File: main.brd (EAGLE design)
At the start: 50.8 x 50.8 mm, 84 parts, among them Q1 5.8A/30V/35mΩ, Q2 5.8A/30V/35mΩ, Q3 2.5A/30V/105mΩ, U2 SN65HVD32_D_8

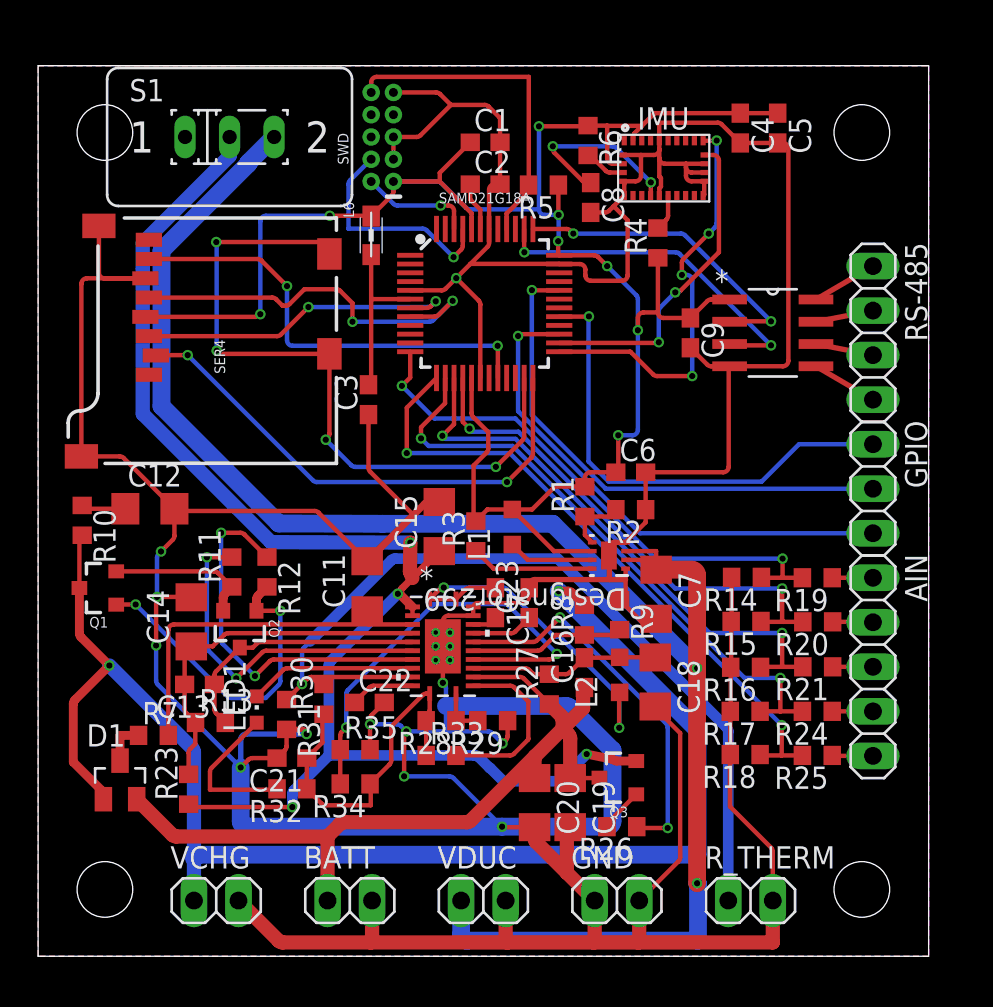
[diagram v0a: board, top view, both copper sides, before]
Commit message: Reworked Layout, added thermocouple ics
Second attempt at a board layout, more balanced spacing.
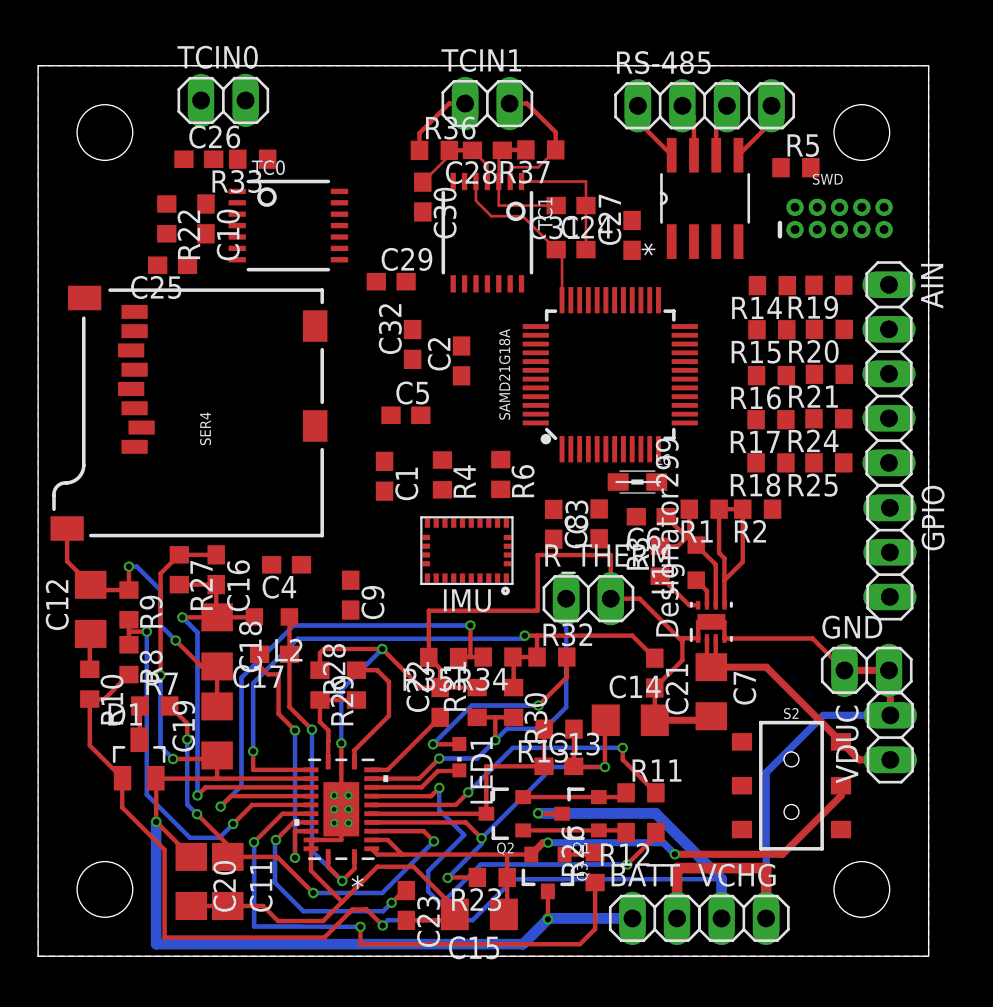
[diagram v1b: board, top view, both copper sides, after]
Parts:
- removed S1: (no value), switch:M251
- added C10, C24, C27, C28, C29, C32: 100nF, resistor:C0603
- added C25, C26, C30, C31: 10nF, resistor:C0603
- added R22, R36, R37: 100, resistor:R0603
- added S2: (no value), SparkFun-Switches:SWITCH_DPDT_SMD_AYZ0202
- added TC0, TC1: MAX31856, microbuilder:TSSOP14
- added TCIN0, TCIN1: (no value), pinhead:1X02
- R33: value 0 -> 100
- moved C4 35.9 mm to (14.2, 22.3), turned to 180 degrees
- moved R33 35.7 mm to (12.2, 45.5), turned to 180 degrees
- moved Q1 30.4 mm to (31.0, 8.13)
- moved VCHG 30.1 mm to (40.3, 2.16)
- moved R9 28.0 mm to (5.18, 20.0)
- moved C5 26.8 mm to (21.0, 30.9), turned to 0 degrees
- moved R11 26.5 mm to (34.4, 9.32), turned to 0 degrees
- moved SWD 26.5 mm to (45.7, 42.1), turned to 0 degrees
- moved R8 26.1 mm to (5.18, 16.9), turned to 270 degrees
- moved R12 26.0 mm to (34.4, 7.06), turned to 180 degrees
- moved C14 25.7 mm to (33.8, 13.5), turned to 0 degrees
- moved C18 25.1 mm to (10.2, 17.9)
- moved VDUC 25.0 mm to (48.6, 12.5), turned to 90 degrees
- moved IMU 24.5 mm to (24.5, 23.1), turned to 180 degrees
- moved C9 24.5 mm to (17.8, 20.6)
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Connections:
- removed net PC_CELL: POWER_CONTROLLER.14, R33.2
- new net N$21: C10.1, C26.2, R33.2, TC0.3
- new net N$22: C10.2, C25.1, R22.2, TC0.4
- new net N$23: R33.1, TC0.2, TCIN0.2
- new net N$24: R22.1, TCIN0.1
- new net N$25: C28.1, C31.2, R37.2, TC1.3
- new net N$26: C28.2, C30.1, R36.2, TC1.4
- new net N$27: R37.1, TC1.2, TCIN1.2
- new net N$28: R36.1, TCIN1.1
- new net TC0_CS: TC0.9
- new net TC0_DRDY: TC0.7
- new net TC0_FAULT: TC0.13
- new net TC1_CS: TC1.9
- new net TC1_DRDY: TC1.7
- new net TC1_FAULT: TC1.13
- net 3.3V: now also C24.1, C27.1, C29.1, C32.1, TC0.5, TC0.8, TC1.5, TC1.8
- net AIN0: no longer SAMD21G18A.12
- net AIN1: no longer SAMD21G18A.16
- net AIN2: no longer SAMD21G18A.15
- net AIN3: no longer SAMD21G18A.14
- net AIN4: no longer SAMD21G18A.13
- net GND: now also C24.2, C25.2, C26.1, C27.2, C29.2, C30.2, C31.1, C32.2, TC0.1, TC0.14, TC1.1, TC1.14
- net GPIO1: no longer SAMD21G18A.29
- net GPIO2: no longer SAMD21G18A.32
- net GPIO3: no longer SAMD21G18A.27
- net PB08D_SER4_P0: now also TC0.12, TC1.12
- net PB09D_SER4_P1: now also TC0.10, TC1.10
- net PB11D_SER4_P3: now also TC0.11, TC1.11
- net PC_PVCC: now also S2.2; no longer S1.2
- net PC_VREF: now also POWER_CONTROLLER.14; no longer R33.1
- net VSYS: now also S2.1; no longer S1.3
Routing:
- net GND: track 359.1 -> 154.6 mm, vias 12 -> 4
- net 3.3V: track 116.9 -> 19.6 mm, vias 8 -> 0
- net VSYS: track 98.2 -> 15.9 mm, vias 2 -> 0
- net PC_PVCC: track 82.6 -> 35.0 mm, vias 4 -> 2
- net PA14_PORT: track 40.7 -> 0.00 mm, vias 4 -> 0
- net AIN4: track 37.0 -> 0.00 mm, vias 2 -> 0
- net AIN3: track 34.5 -> 0.00 mm, vias 2 -> 0
- net AIN2: track 32.0 -> 0.00 mm, vias 2 -> 0
- net AIN0: track 31.4 -> 0.00 mm, vias 2 -> 0
- net GPIO2: track 29.9 -> 0.00 mm, vias 1 -> 0
- net GPIO3: track 29.8 -> 0.00 mm, vias 1 -> 0
- net PA15_PORT: track 29.5 -> 0.00 mm, vias 2 -> 0
- net AIN1: track 29.0 -> 0.00 mm, vias 2 -> 0
- net PC_TS: track 50.7 -> 22.4 mm, vias 1 -> 2
- net GPIO1: track 27.6 -> 0.00 mm, vias 1 -> 0
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
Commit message: Some fixes, layout additions
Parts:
- added R38, R39: 1k, resistor:R0603
- added R40: 10k, resistor:R0603
- moved C26 5.95 mm to (15.1, 45.2), turned to 180 degrees
- moved TCIN0 5.94 mm to (16.5, 48.7)
- moved R6 4.56 mm to (30.0, 24.7)
- moved C8 4.50 mm to (26.0, 27.6), turned to 90 degrees
- moved L6 4.11 mm to (38.3, 27.5)
- moved R22 3.01 mm to (8.69, 44.8)
- moved C29 2.41 mm to (21.8, 36.7), turned to 270 degrees
- moved C32 2.37 mm to (19.7, 33.2)
- moved TC0 2.11 mm to (16.3, 41.2)
- moved C2 2.04 mm to (22.5, 32.8), turned to 180 degrees
- moved C25 1.76 mm to (7.32, 41.1), turned to 270 degrees
- moved C10 1.76 mm to (11.3, 41.9), turned to 180 degrees
- moved SAMD21G18A 1.61 mm to (34.2, 33.7)
- moved C9 1.60 mm to (16.5, 19.7)
- moved R33 1.27 mm to (11.3, 44.7), turned to 270 degrees
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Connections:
- net 3.3V: now also R38.1, R39.1, R40.2
- net AIN0: now also SAMD21G18A.16
- net AIN1: now also SAMD21G18A.15
- net AIN2: now also SAMD21G18A.14
- net AIN3: now also SAMD21G18A.13
- net AIN4: now also SAMD21G18A.12
- net GND: now also SER4.CD2
- net PA14_PORT: now also R40.1; no longer SER4.CD2
- net PA16_SER1_I2C_SDA: now also R38.2
- net PA17_SER1_I2C_SCL: now also R39.2
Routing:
- net GND: track 154.6 -> 167.8 mm
- net AIN4: track 0.00 -> 10.6 mm, vias 0 -> 2
- net AIN0: track 0.00 -> 10.2 mm, vias 0 -> 2
- net AIN1: track 0.00 -> 9.08 mm, vias 0 -> 2
- net AIN2: track 0.00 -> 8.59 mm, vias 0 -> 2
- net AIN3: track 0.00 -> 8.51 mm, vias 0 -> 2
- net N$8: track 0.00 -> 2.59 mm
- net N$4: track 0.00 -> 2.59 mm
- net N$5: track 0.00 -> 2.58 mm
- net N$3: track 0.00 -> 2.56 mm
- net N$1: track 0.00 -> 2.55 mm
- net 3.3V: track 19.6 -> 17.0 mm

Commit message: More layout additions
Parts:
- moved C30 2.90 mm to (20.0, 45.5), turned to 90 degrees
- moved R39 1.27 mm to (19.3, 22.3)
- moved C25 0.76 mm to (8.08, 41.2)
- moved C10 0.73 mm to (10.6, 42.1)
- moved R38 0.60 mm to (19.3, 19.8)
- moved R22 0.59 mm to (8.10, 44.8)
- moved R5 0.54 mm to (42.7, 45.1)
- moved C5 0.33 mm to (20.9, 30.4)
- moved R33 0.23 mm to (11.5, 44.7)
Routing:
- net 3.3V: track 17.0 -> 68.2 mm, vias 0 -> 2
- net GND: track 167.8 -> 216.7 mm
- net PB08D_SER4_P0: track 0.00 -> 48.7 mm, vias 0 -> 4
- net PB09D_SER4_P1: track 0.00 -> 43.7 mm, vias 0 -> 4
- net PB11D_SER4_P3: track 0.00 -> 41.8 mm, vias 0 -> 4
- net N$23: track 0.00 -> 17.7 mm, vias 0 -> 2
- net MCU_TX: track 0.00 -> 14.8 mm, vias 0 -> 2
- net MCU_RX: track 0.00 -> 11.7 mm, vias 0 -> 2
- net N$2: track 0.00 -> 10.3 mm
- net N$24: track 0.00 -> 8.41 mm
- net N$22: track 0.00 -> 8.27 mm
- net N$21: track 0.00 -> 7.92 mm
- net SWD_NRES: track 0.00 -> 7.79 mm, vias 0 -> 1
- net VDDCORE: track 0.00 -> 6.83 mm
- net NRESET: track 0.00 -> 3.99 mm
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
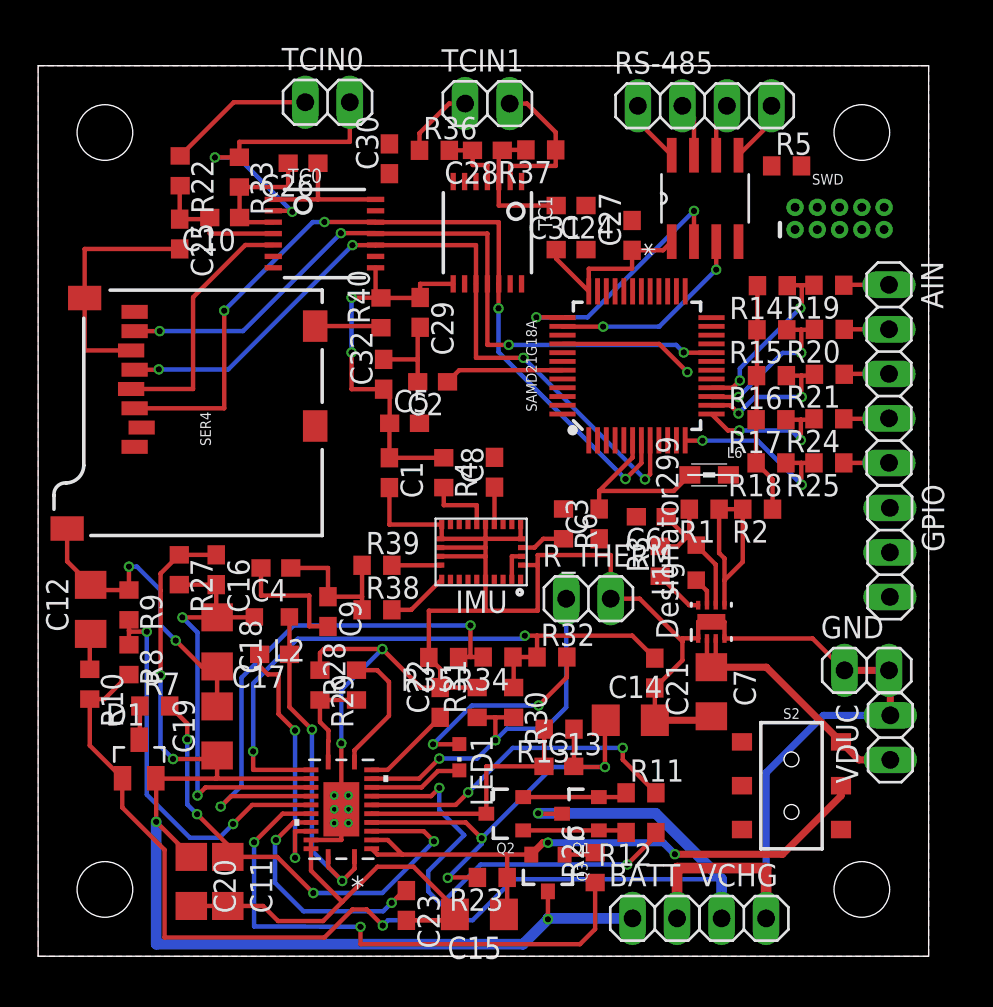
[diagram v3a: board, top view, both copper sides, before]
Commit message: Finished 2nd layout
Still needs a few error corrections and status leds where possible.
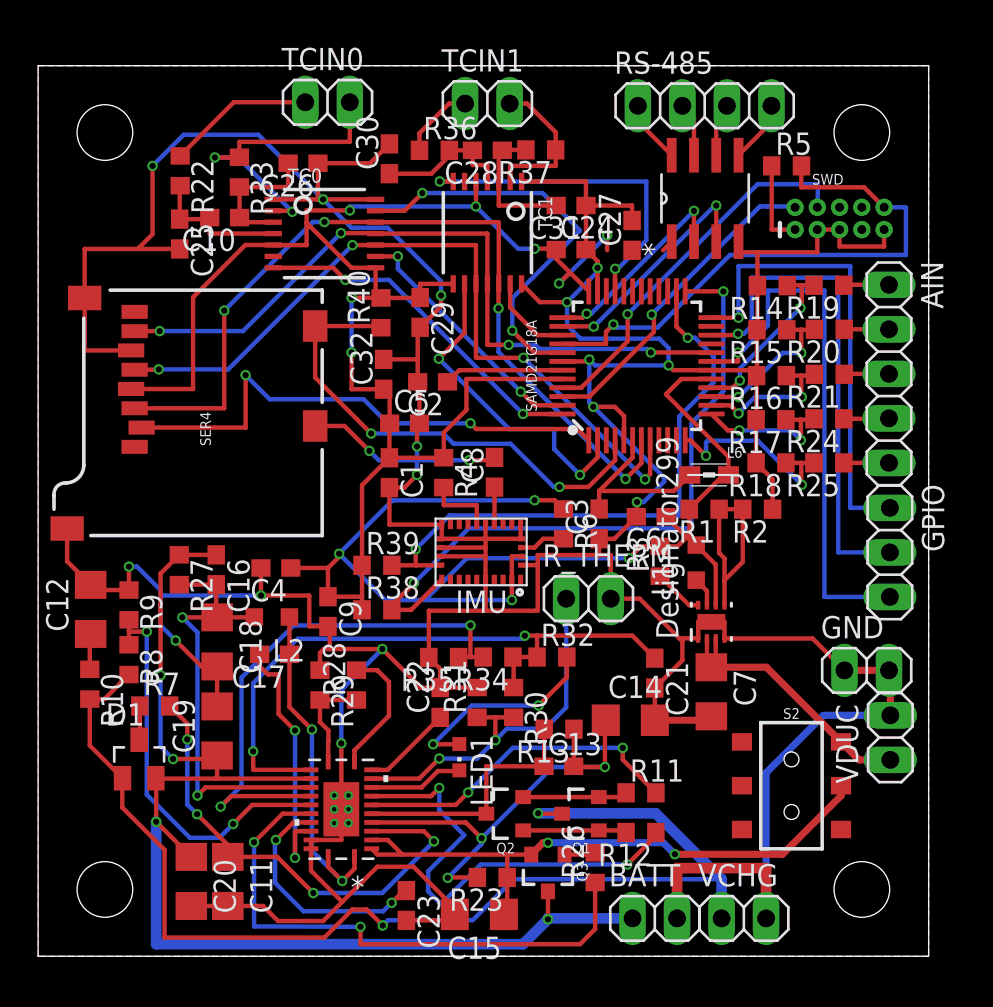
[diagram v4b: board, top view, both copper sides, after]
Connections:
- removed net PA14_PORT: R40.1, SAMD21G18A.23, SER4.CD1
- removed net PA15_PORT: SAMD21G18A.24, SER4.CS
- new net SD_CD: R40.1, SAMD21G18A.4, SER4.CD1
- new net SD_CS: SAMD21G18A.1, SER4.CS
- net GPIO1: now also SAMD21G18A.24
- net GPIO2: now also SAMD21G18A.22
- net GPIO3: now also SAMD21G18A.19
- net TC0_CS: now also SAMD21G18A.47
- net TC0_DRDY: now also SAMD21G18A.48
- net TC0_FAULT: now also SAMD21G18A.41
- net TC1_CS: now also SAMD21G18A.2
- net TC1_DRDY: now also SAMD21G18A.33
- net TC1_FAULT: now also SAMD21G18A.39
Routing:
- net GND: track 216.7 -> 347.6 mm, vias 4 -> 18
- net 3.3V: track 68.2 -> 169.6 mm, vias 2 -> 11
- net PA16_SER1_I2C_SDA: track 3.56 -> 39.2 mm, vias 0 -> 2
- net PA17_SER1_I2C_SCL: track 2.79 -> 34.3 mm, vias 0 -> 2
- net GPIO3: track 0.00 -> 30.8 mm, vias 0 -> 1
- net SD_CS: track 0.00 -> 30.0 mm, vias 0 -> 2
- net GPIO2: track 0.00 -> 28.8 mm, vias 0 -> 1
- net SD_CD: track 0.00 -> 28.3 mm, vias 0 -> 2
- net GPIO1: track 0.00 -> 26.9 mm, vias 0 -> 1
- net SWD_NRES: track 7.79 -> 32.6 mm
- net TC0_FAULT: track 0.00 -> 23.7 mm, vias 0 -> 2
- net PA30_SWCLK: track 0.00 -> 21.6 mm, vias 0 -> 1
- net TC0_DRDY: track 0.00 -> 20.0 mm, vias 0 -> 2
- net TC1_DRDY: track 0.00 -> 19.6 mm, vias 0 -> 2
- net TC1_CS: track 0.00 -> 18.7 mm, vias 0 -> 2
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
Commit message: Fixed some air wires
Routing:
- net 3.3V: track 169.6 -> 181.5 mm
- net PC_VREF: track 44.8 -> 49.6 mm, vias 2 -> 3
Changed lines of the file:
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@@
 <wire x1="43.561" y1="26.8986" x2="41.0464" y2="29.4132" width="0.254" layer="16"/>
 <wire x1="41.0464" y1="29.4132" x2="38.2016" y2="29.4132" width="0.254" layer="16"/>
-<wire x1="38.2016" y1="29.4132" x2="37.8968" y2="29.4132" width="0" layer="19" extent="1-16"/>
 <wire x1="36.9302" y1="29.4132" x2="36.913" y2="29.4304" width="0.254" layer="1"/>
 <wire x1="36.913" y1="29.4304" x2="37.2192" y2="29.4304" width="0.254" layer="1"/>
@@
 <wire x1="17.8816" y1="37.5666" x2="19.431" y2="37.5666" width="0.254" layer="1"/>
 <wire x1="19.431" y1="37.5666" x2="19.431" y2="37.553" width="0.254" layer="1"/>
-<wire x1="35.6498" y1="40.2726" x2="36.1442" y2="40.767" width="0.254" layer="1"/>
 <wire x1="29.5538" y1="40.3098" x2="29.5538" y2="39.7896" width="0.254" layer="1"/>
 <wire x1="29.5538" y1="39.7896" x2="30.3283" y2="39.0151" width="0.254" layer="1"/>
@@
 <wire x1="18.4794" y1="26.8732" x2="20.0406" y2="28.4344" width="0.254" layer="1"/>
 <wire x1="43.18" y1="41.4528" x2="41.8474" y2="41.4528" width="0.254" layer="1"/>
-<wire x1="41.8474" y1="41.4528" x2="41.8474" y2="45.085" width="0.254" layer="1"/>
-<wire x1="32.4612" y1="40.2726" x2="32.4612" y2="41.1226" width="0.254" layer="1"/>
+<wire x1="41.8474" y1="41.4528" x2="41.8474" y2="43.4848" width="0.254" layer="1"/>
+<wire x1="41.8474" y1="43.4848" x2="41.8474" y2="45.085" width="0.254" layer="1"/>
+<wire x1="32.4612" y1="41.1226" x2="32.4612" y2="40.2726" width="0.254" layer="1"/>
 <via x="32.4612" y="41.1226" extent="1-16" drill="0.35"/>
 <wire x1="32.4612" y1="41.1226" x2="29.718" y2="38.3794" width="0.254" layer="16"/>
@@
 <wire x1="29.503" y1="40.3606" x2="29.5538" y2="40.3098" width="0.254" layer="1"/>
 <contactref element="C27" pad="1"/>
-<wire x1="36.1442" y1="40.767" x2="41.8474" y2="41.4528" width="0" layer="19" extent="1-1"/>
-<wire x1="33.8836" y1="40.2726" x2="35.6498" y2="40.2726" width="0" layer="19" extent="1-1"/>
-<wire x1="32.4612" y1="40.2726" x2="33.8836" y2="40.2726" width="0" layer="19" extent="1-1"/>
+<wire x1="32.4612" y1="40.2726" x2="33.8836" y2="40.2726" width="0.254" layer="1"/>
+<wire x1="41.8474" y1="43.4848" x2="36.1442" y2="43.4848" width="0.254" layer="1"/>
+<wire x1="36.1442" y1="43.4848" x2="36.1442" y2="40.767" width="0.254" layer="1"/>
+<wire x1="33.8836" y1="40.2726" x2="36.1442" y2="40.2726" width="0.254" layer="1"/>
+<wire x1="36.1442" y1="40.2726" x2="36.1442" y2="40.767" width="0.254" layer="1"/>
 </signal>
 <signal name="GND">
@@
 <contactref element="VDUC" pad="2"/>
 <contactref element="GND" pad="2"/>
-<polygon width="0.254" layer="16">
+<polygon width="0.2032" layer="16" isolate="0.254">
 <vertex x="0" y="50.8"/>
 <vertex x="50.8" y="50.8"/>
@@
 <vertex x="0" y="0"/>
 </polygon>
-<polygon width="0.254" layer="1">
+<polygon width="0.2032" layer="1" isolate="0.254">
 <vertex x="0" y="50.8"/>
 <vertex x="50.8" y="50.8"/>
@@
 <wire x1="12.2682" y1="10.632" x2="12.2682" y2="11.684" width="0.254" layer="1"/>
 <via x="12.2682" y="11.684" extent="1-16" drill="0.35"/>
-<wire x1="12.2682" y1="11.684" x2="12.2682" y2="15.5702" width="0.254" layer="16"/>
+<wire x1="12.2682" y1="15.5702" x2="12.2682" y2="11.684" width="0.254" layer="16"/>
 <wire x1="12.2682" y1="15.5702" x2="14.8082" y2="18.1102" width="0.254" layer="16"/>
 <wire x1="27.7622" y1="18.1102" x2="27.7622" y2="18.288" width="0.254" layer="16"/>
@@
 <wire x1="27.7622" y1="18.288" x2="28.4616" y2="18.288" width="0.254" layer="1"/>
 <wire x1="28.4616" y1="18.288" x2="28.4616" y2="17.0688" width="0.254" layer="1"/>
-<wire x1="14.8082" y1="18.1102" x2="27.7622" y2="18.1102" width="0.254" layer="16"/>
+<wire x1="14.8082" y1="18.1102" x2="21.1836" y2="18.1102" width="0.254" layer="16"/>
+<wire x1="21.1836" y1="18.1102" x2="27.7622" y2="18.1102" width="0.254" layer="16"/>
 <wire x1="28.4616" y1="17.0688" x2="27.1272" y2="17.0688" width="0.254" layer="1"/>
 <wire x1="27.1272" y1="17.0688" x2="27.0882" y2="17.0688" width="0.254" layer="1"/>
@@
 <wire x1="35.179" y1="17.0044" x2="33.8954" y2="18.288" width="0.254" layer="1"/>
 <wire x1="33.8954" y1="18.288" x2="28.4616" y2="18.288" width="0.254" layer="1"/>
-<wire x1="15.5664" y1="10.632" x2="18.0474" y2="11.078" width="0" layer="19" extent="1-1"/>
+<wire x1="21.1836" y1="18.1102" x2="21.1836" y2="14.8844" width="0.254" layer="16"/>
+<wire x1="21.1836" y1="14.8844" x2="20.0152" y2="13.716" width="0.254" layer="16"/>
+<via x="20.0152" y="13.716" extent="1-16" drill="0.35"/>
 </signal>
 <signal name="PC_BTST">

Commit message: A few spacing adjustments
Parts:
- moved GND 4.27 mm to (43.5, 18.3)
- moved VDUC 4.22 mm to (48.6, 16.7)
- moved S2 1.69 mm to (44.1, 10.9)
- moved C20 0.53 mm to (8.20, 4.27)
- moved R16 0.27 mm to (42.1, 33.2)
- moved R17 0.26 mm to (42.1, 30.7)
- moved R18 0.25 mm to (42.1, 28.1)
- moved C11 0.23 mm to (11.0, 4.29)
- moved R15 0.23 mm to (42.1, 35.8)
- moved R14 0.20 mm to (42.1, 38.3)
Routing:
- net PC_PVCC: track 35.0 -> 38.2 mm
- net GND: track 347.6 -> 345.4 mm, vias 18 -> 19
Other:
- outline, holes or cut-outs redrawn
